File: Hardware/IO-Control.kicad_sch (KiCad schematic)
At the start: 42 parts, among them J1 Molex 047053-1000, J2 S3B-XH-A, P6 TYPE-C-31-M-12, Q1 MMBT3904, Q2 MMBT3904, Q3 PMV16XNR, Q4 MMBT3904, SW1 RESET, SW2 FLASH, U8 CH340G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

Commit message: finally created part for pushbutton
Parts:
- SW1, SW2: footprint (none) -> PersonalDiscretes:C&K PTS636-G
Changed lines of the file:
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@@
       (effects (font (size 1.27 1.27)) (justify right))
     )
-    (property "Footprint" "" (id 2) (at 44.45 175.26 0)
+    (property "Footprint" "PersonalDiscretes:C&K PTS636-G" (id 2) (at 44.45 175.26 0)
       (effects (font (size 1.27 1.27)) hide)
     )
@@
       (effects (font (size 1.27 1.27)) (justify right))
     )
-    (property "Footprint" "" (id 2) (at 102.87 179.07 0)
-      (effects (font (size 1.27 1.27)) hide)
-    )
+    (property "Footprint" "PersonalDiscretes:C&K PTS636-G" (id 2) (at 102.87 179.07 0)
+      (effects (font (size 1.27 1.27)) hide)
+    )

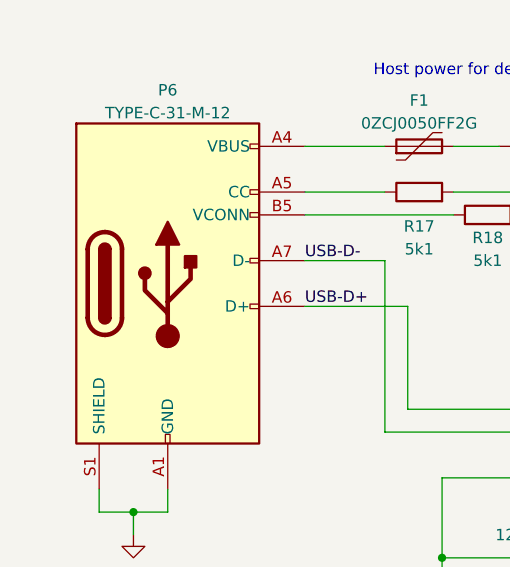
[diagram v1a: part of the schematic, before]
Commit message: updated to new KiCAD format
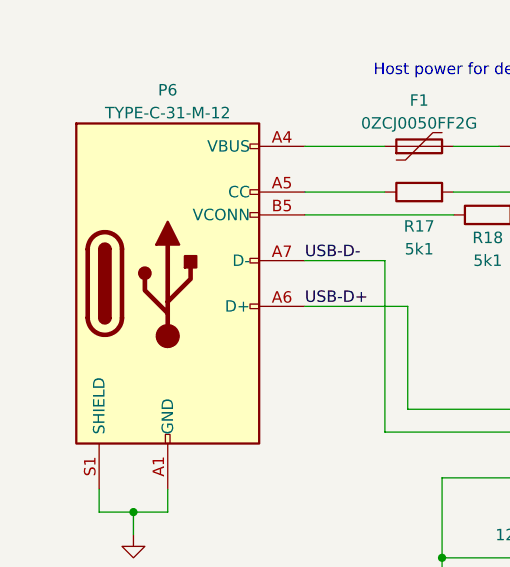
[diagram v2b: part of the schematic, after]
